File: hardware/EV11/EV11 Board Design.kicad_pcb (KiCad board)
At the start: 4 copper layers, 66 x 99.3 mm, 107 parts, among them CN1 PJ-313E-8A_C707222, CN2 X1270WVS-2X05B-6TV01, CN3 WAFER-SH1.0-6PWB, CN4 WAFER-SH1.0-6PWB, J1 Conn_01x02_Socket, J10 Conn_01x08_Socket, J9 USB_C_Receptacle, SW1 TS-1037-A11B3-D2, SW2 MSK12C02-HB, SW3 TS-1037-A11B3-D2, SW4 SW_Push, SW5 SW_Push, U1 STM32F405RGTx, U11 ESP32-S3-WROOM-1-N8R2, U13 BM14B(0.8)-24DS-0.4V(53), U2 BQ21040DBVR, U3 CH340C, U4 USBLC6-2P6, U6 WM8960CGEFL/RV, U7 TPS63060, U8 STM32F072C8T6, Y1 Crystal_GND24

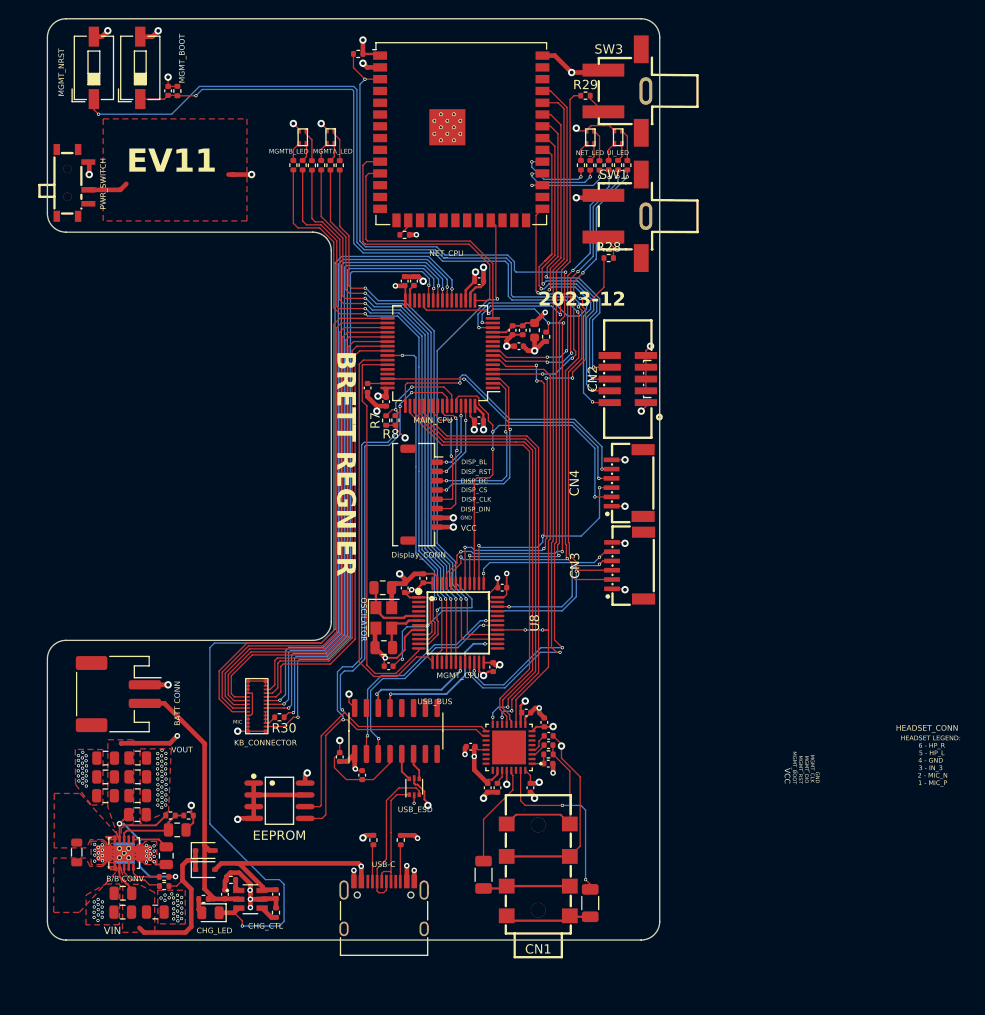
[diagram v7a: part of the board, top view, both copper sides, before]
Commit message: Updated silk screen
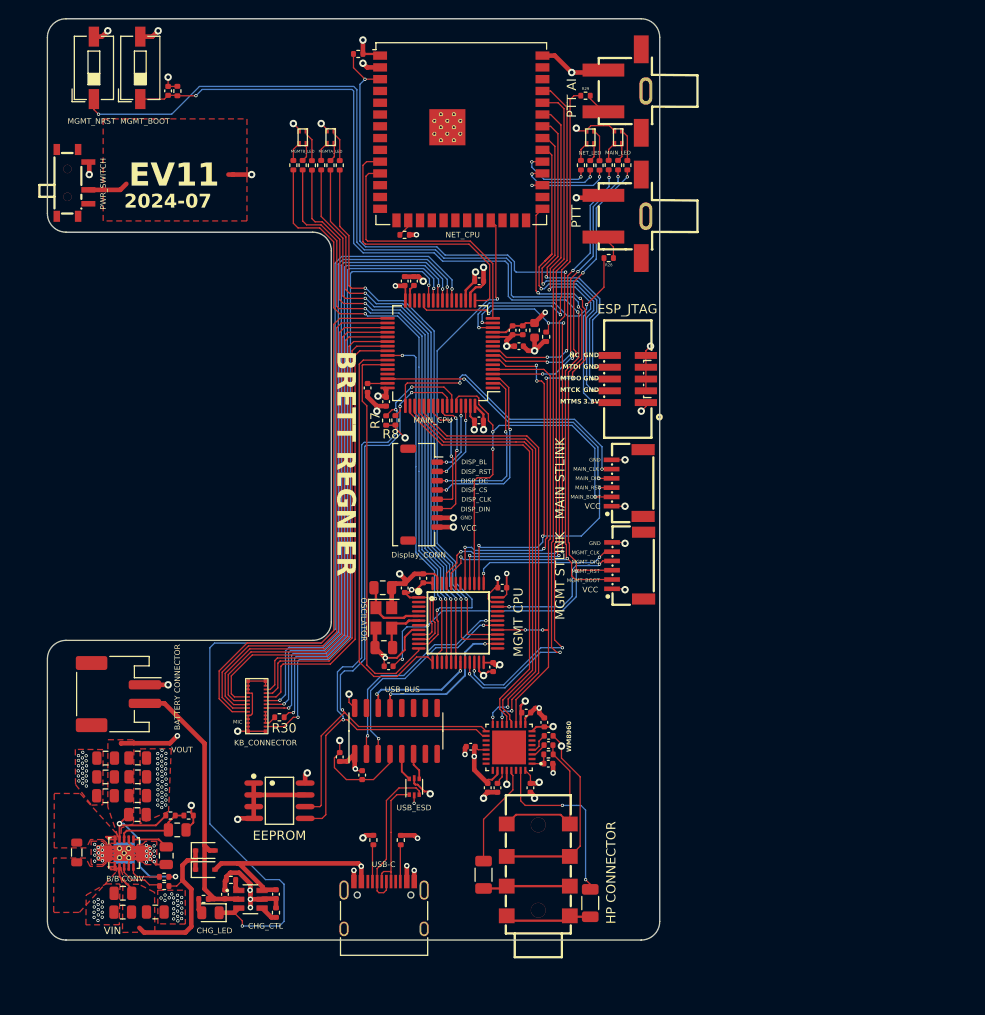
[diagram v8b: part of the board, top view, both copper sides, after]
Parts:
- HP CONNECTOR: renamed from CN1
- MAIN STLINK: renamed from CN4
- MGMT CPU: renamed from U8
- MGMT STLINK: renamed from CN3
- PTT AI: renamed from SW3
- renumbered CN2 to ESP_JTAG, SW1 to PTT
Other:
- board text added: "2024-07"
- board text added: "3.3V"
- board text added: "BATTERY CONNECTOR"
- board text added: "MAIN_BOOT"
- board text added: "MAIN_CLK"
- board text added: "MAIN_DIO"
- board text added: "MAIN_LED"
- board text added: "MAIN_RST"
- board text added: "MTCK"
- board text added: "MTDI"
- board text added: "MTDO"
- board text added: "MTMS"
- board text added: "NC"
- board text added: "WM8960"
- board text removed: "2023-12"
- board text removed: "BATT CONN"
- board text removed: "HEADSET LEGEND: 6 - HP_R 5 - HP_L 4 - GND 3 - IN_3 2 - MIC_N 1 - MIC_P"
- board text removed: "HEADSET_CONN"
- board text removed: "MGMT_CPU"
- board text removed: "UI_LED"
